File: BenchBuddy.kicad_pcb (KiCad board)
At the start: 4 copper layers, 165.1 x 63.5 mm, 0 parts

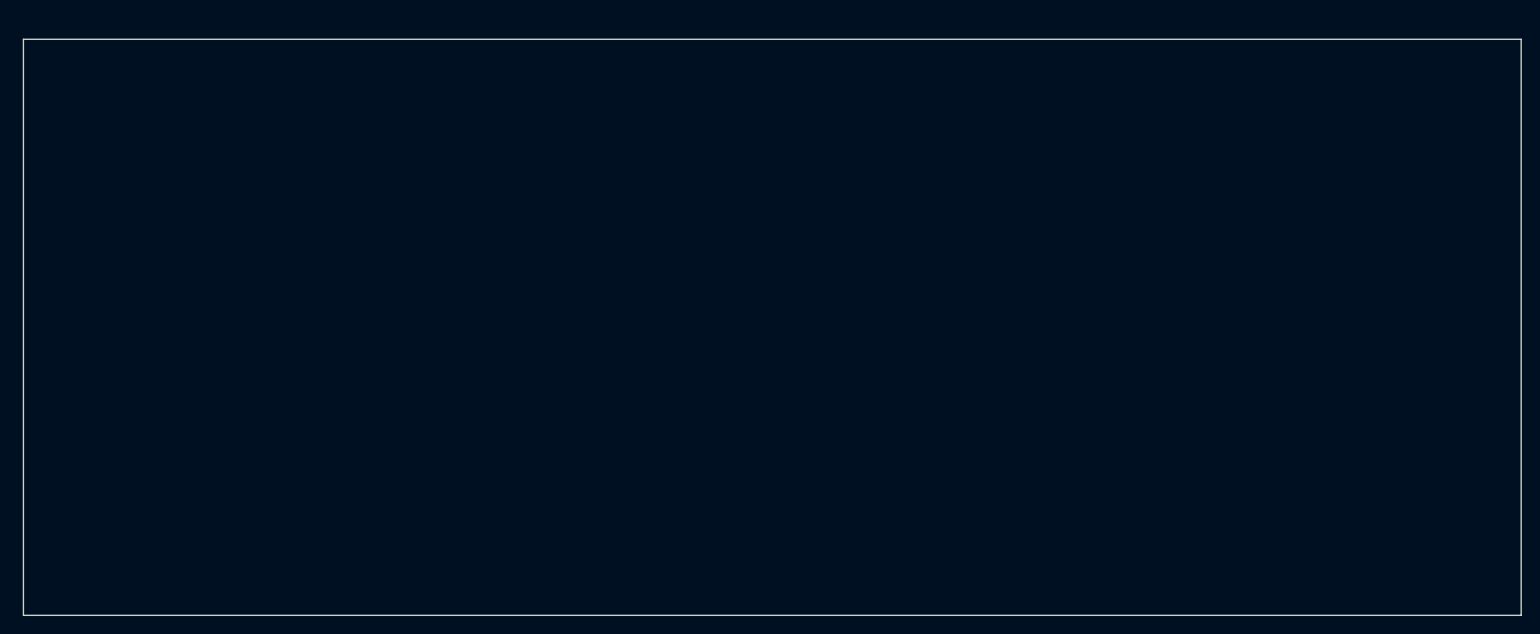
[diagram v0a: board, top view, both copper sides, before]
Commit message: Nach Einfuegen Relay-Modul
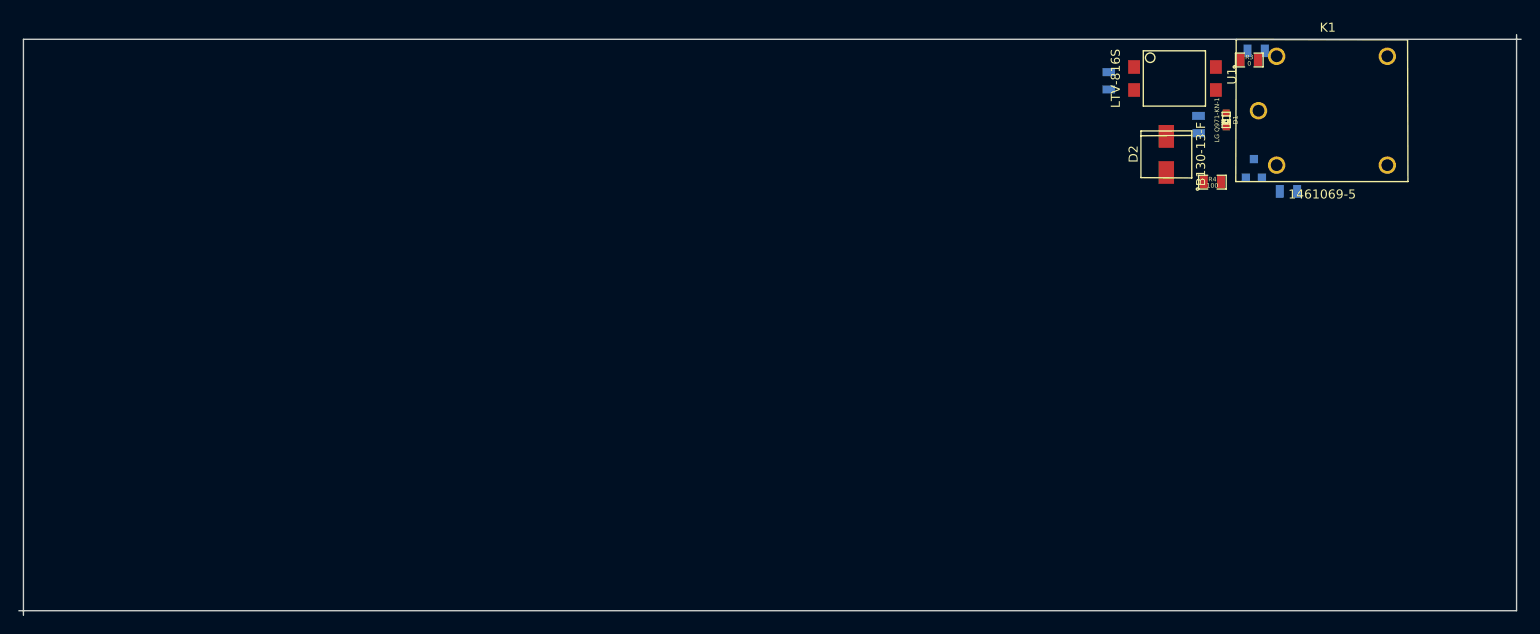
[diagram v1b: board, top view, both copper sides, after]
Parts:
- added D1: LG Q971-KN-1, LED-0603, F.Cu at (244.9, 75.9)
- added D2: B130-13-F, SMA, F.Cu at (238.3, 79.8)
- added K1: 1461069-5, TE-SPDT, F.Cu at (248.4, 74.9)
- added Q1: 2N3904, SOT23EBC, B.Cu at (247.9, 81.3)
- added R1: 500, SM0805, B.Cu at (231.9, 71.6)
- added R2: 200, SM0805, B.Cu at (241.8, 76.5)
- added R3: 0, SM0805, F.Cu at (247.4, 69.3)
- added R4: 100, SM0805, F.Cu at (243.3, 82.8)
- added R5: 0, SM0805, B.Cu at (248.2, 68.3)
- added R6: 0, SM0805, B.Cu at (251.7, 83.8)
- added U1: LTV-816S, 4-SMD, F.Cu at (234.7, 70.1)
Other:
- board size 165.1 x 63.5 mm -> 165.6 x 64 mm

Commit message: Am Ende der 5. Woche.
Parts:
- added ARD1: ARDUINO, Arduino, B.Cu at (147.8, 98.6)
- added C1: C, SM0805, F.Cu at (120.1, 104.4)
- added C10: C, SM0805, F.Cu at (236.0, 82.0)
- added C11: C, SM0805, F.Cu at (120.1, 101.9)
- added C12: C, SM0805, F.Cu at (136.9, 90.7)
- added C13: C, SM0805, F.Cu at (136.4, 87.6)
- added C14: C, SM0805, F.Cu at (141.5, 106.2)
- added C15: C, SM0805, B.Cu at (164.8, 50.3)
- added C16: C, SM0805, B.Cu at (189.2, 147.3)
- added C17: C, SM0805, F.Cu at (225.6, 93.5)
- added C18: C, SM0805, F.Cu at (142.0, 113.3)
- added C19: C, SM0805, B.Cu at (159.5, 47.8)
- added C2: C, SM1206, F.Cu at (137.4, 103.1)
- added C20: C, SM0805, F.Cu at (147.6, 91.9)
- added C21: C, SM0805, B.Cu at (187.2, 155.4)
- added C22: C, SM0805, F.Cu at (145.8, 104.4)
- added C23: C, SM0805, B.Cu at (163.1, 47.5)
- added C24: C, SM0805, F.Cu at (138.9, 83.3)
- added C25: C, SM0805, F.Cu at (146.3, 94.2)
- added C3: C, SM1206, F.Cu at (137.7, 111.0)
- added C4: 1u, SM1206, F.Cu at (136.1, 94.2)
- added C5: 1u, SM0805, B.Cu at (77.5, 28.2)
- added C6: C, SM0805, B.Cu at (222.2, 70.4)
- added C7: C, SM0805, B.Cu at (224.0, 81.5)
- added C8: C, SM0805, B.Cu at (221.5, 81.8)
- added C9: C, SM0805, F.Cu at (233.7, 89.4)
- added D10: MMBD914-7-F, SOT23_Diode, F.Cu at (148.8, 109.7)
- added D12: MMBD914-7-F, SOT23_Diode, F.Cu at (143.3, 83.6)
- added D13: MMBD914-7-F, SOT23_Diode, F.Cu at (193.3, 145.8)
- added D14: MMBD914-7-F, SOT23_Diode, F.Cu at (162.3, 62.0)
- added D15: MMBD914-7-F, SOT23_Diode, F.Cu at (184.2, 149.6)
- added D4: B0540WS-7, SOD-323, F.Cu at (70.4, 29.5)
- added D5: B130-13-F, SMA, F.Cu at (260.9, 87.6)
- added D7: MMBD914-7-F, SOT23_Diode, F.Cu at (168.7, 53.3)
- added D8: MMBD914-7-F, SOT23_Diode, F.Cu at (150.4, 102.4)
- added D9: MMBD914-7-F, SOT23_Diode, F.Cu at (156.7, 51.1)
- added L1: CM322522-220KL, SM1210L, F.Cu at (119.1, 111.3)
- added L2: CM322522-220KL, SM1210L, F.Cu at (137.7, 121.7)
- added L3: CM322522-220KL, SM1210L, F.Cu at (118.4, 90.2)
- added L4: 22u, NR4012, F.Cu at (82.0, 26.9)
- added P1: 24 Pin MiniFit JR, ATX_Header, F.Cu at (118.1, 74.9)
- added P2: CONN_3X2, pin_array_3x2, F.Cu at (231.4, 63.0)
- added P3: CONN_2, PIN_ARRAY_2X1, F.Cu at (216.4, 76.7)
- added P4: 12 Pin Terminal Block, 12PinTB, F.Cu at (273.6, 87.1)
- added P5: 3 Pin TB, 3PinTB, F.Cu at (272.8, 125.5)
- added Q2: DMN65D8L-7, SOT23GDS, F.Cu at (236.7, 85.6)
- added Q3: AOD476, DPAK2, F.Cu at (265.4, 82.3)
- added Q4: AOD476, DPAK2, F.Cu at (257.0, 82.3)
- added R10: R, SM1206, B.Cu at (238.8, 77.2)
- added R11: R, SM0805, F.Cu at (242.1, 70.9)
- added R12: R, SM0805, B.Cu at (228.9, 67.8)
- added R13: R, SM0805, B.Cu at (228.9, 71.9)
- added R14: R, SM0805, F.Cu at (145.3, 118.4)
- added R15: 15, SM0805, F.Cu at (265.7, 58.4)
- added R16: R, SM1206, B.Cu at (230.6, 84.3)
- added R17: R, SM0805, B.Cu at (155.4, 98.8)
- added R18: R, SM0805, F.Cu at (142.7, 101.9)
- added R19: R, SM0805, F.Cu at (142.0, 108.7)
- added R20: 5k, EVUE3k, F.Cu at (213.1, 54.6)
- added R21: 715, SM0805, B.Cu at (164.3, 53.6)
- added R22: R, SM0805, B.Cu at (161.0, 53.3)
- added R23: R, SM0805, F.Cu at (146.1, 98.8)
- added R24: R, SM0805, F.Cu at (150.6, 98.6)
- added R25: R, SM0805, B.Cu at (182.9, 153.7)
- added R26: R, SM0805, F.Cu at (151.4, 120.1)
- added R27: R, SM0805, F.Cu at (153.9, 120.1)
- added R28: R, SM0805, F.Cu at (156.5, 120.1)
- added R29: R, SM0805, F.Cu at (159.0, 120.1)
- added R30: R, SM0805, F.Cu at (164.1, 120.1)
- added R31: R, SM0805, F.Cu at (166.6, 120.1)
- added R32: R, SM0805, F.Cu at (169.2, 120.1)
- added R33: R, SM0805, F.Cu at (171.7, 120.1)
- added R34: R, SM0805, F.Cu at (142.2, 78.5)
- added R35: R, SM0805, F.Cu at (144.8, 78.5)
- added R36: R, SM0805, F.Cu at (147.3, 78.5)
- added R37: R, SM0805, F.Cu at (149.9, 78.5)
- added R38: R, SM0805, F.Cu at (152.4, 78.5)
- added R39: R, SM0805, F.Cu at (154.9, 78.5)
- added R40: R, SM0805, F.Cu at (159.0, 78.5)
- added R41: R, SM0805, F.Cu at (174.2, 78.5)
- added R42: R, SM0805, F.Cu at (176.8, 78.5)
- added R43: R, SM0805, F.Cu at (218.4, 50.0)
- added R44: R, SM0805, B.Cu at (231.6, 67.8)
- added R45: R, SM0805, B.Cu at (234.2, 67.8)
- added R46: R, SM0805, F.Cu at (164.1, 78.5)
- added R47: R, SM0805, F.Cu at (166.6, 78.5)
- added R48: 0, SM0805, B.Cu at (225.8, 76.7)
- added R49: 0, SM0805, B.Cu at (225.8, 79.0)
- added R50: R, SM0805, F.Cu at (169.4, 78.5)
- added R51: R, SM0805, F.Cu at (172.0, 78.5)
- added R52: R, SM0805, F.Cu at (141.7, 91.2)
- added R53: R, SM0805, F.Cu at (141.0, 86.9)
- added R54: 715, SM0805, B.Cu at (186.7, 152.9)
- added R55: 5k, EVUE3k, F.Cu at (217.9, 137.7)
- added R7: R, SM1206, B.Cu at (229.4, 77.0)
- added R8: R, SM1206, B.Cu at (232.7, 77.2)
- added R9: R, SM1206, B.Cu at (235.7, 77.2)
- added SW1: PowerSwitch, BB_Switch, F.Cu at (134.4, 127.8)
- added TH1: MINISMDC050F-2, SM1812, B.Cu at (118.4, 116.8)
- added TH2: MINISMDC050F-2, SM1812, B.Cu at (118.9, 110.7)
- added TH3: MINISMDC050F-2, SM1812, B.Cu at (119.1, 83.3)
- added TH4: MINISMDC050F-2, SM1812, B.Cu at (137.4, 117.1)
- added TH5: MINISMDC050F-2, SM1812, F.Cu at (252.7, 87.6)
- added U11: LM317S, TO220, F.Cu at (163.6, 51.6)
- added U2: MCP3901, SSOP20, F.Cu at (223.0, 77.0)
- added U3: LMT84, SOT353, B.Cu at (222.8, 77.5)
- added U4: OPA4170, SO14N, F.Cu at (239.0, 76.5)
- added U5: MCP4801, SO8N, F.Cu at (222.8, 86.6)
- added U6: AP5726, SOT23_6, F.Cu at (73.9, 28.2)
- added U7: LM317S, TO220, F.Cu at (145.3, 109.5)
- added U8: LM337T, TO220, F.Cu at (144.8, 88.1)
- added U9: LM337T, TO220, F.Cu at (189.7, 148.6)
- moved D1 45.6 mm to (247.7, 121.4)
- moved R2 45.6 mm to (244.6, 121.9)
- moved R3 45.6 mm to (250.2, 114.8)
- moved R4 45.6 mm to (246.1, 128.3)
- moved R5 45.6 mm to (251.0, 113.8)
- moved R6 45.6 mm to (254.5, 129.3)
- moved D2 45.6 mm to (241.0, 125.2)
- moved K1 45.6 mm to (251.2, 120.4)
- moved Q1 45.6 mm to (250.7, 126.7)
- moved R1 45.6 mm to (234.7, 117.1)
- moved U1 45.6 mm to (237.5, 115.6)
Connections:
- K1 pad 1: (no net) -> /Relay/RELAY_COM
- K1 pad 3: (no net) -> /Relay/RELAY_NO
- K1 pad 4: (no net) -> /Relay/RELAY_NC
- R1 pad 1: (no net) -> /Arduino/RELAY-
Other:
- board size 165.6 x 64 mm -> 165.1 x 63.8 mm
